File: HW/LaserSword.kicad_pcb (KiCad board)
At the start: 2 copper layers, 25 x 23 mm, 29 parts, among them J1 SWD, J2 INPUTS, J3 OUTPUTS, J4 DEBUG, Q1 Q_PNP_BEC, Q2 Q_PNP_BEC, U1 MMA7660FC, U2 DAC101S101, U3 MKE04Z8VWJ4

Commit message: Refactor to use NPN
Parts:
- Q1, Q2: value Q_PNP_BEC -> Q_NPN_BEC; moved to F.Cu
- R1, R2, R5, R7: moved to B.Cu
- moved R4 7.21 mm to (116.8, 72.3), turned to 270 degrees
- moved R3 6.89 mm to (116.8, 67.6), turned to 270 degrees
- moved R5 1.06 mm to (118.7, 72.3), turned to 90 degrees
- moved R7 1.06 mm to (120.2, 72.3), turned to 90 degrees
- moved Q2 0.91 mm to (118.7, 72.4)
- moved R2 0.82 mm to (120.2, 67.6), turned to 90 degrees
- moved R1 0.78 mm to (118.6, 67.6), turned to 90 degrees
- moved Q1 0.41 mm to (118.7, 67.7)
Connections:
- Q1 pad 2: VCC -> GND
- Q2 pad 2: VCC -> GND
- R3 pad 1: VCC -> GND
- R4 pad 1: VCC -> GND
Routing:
- net GND: track 85.9 -> 105.6 mm, vias 3 -> 5
- net VCC: track 98.7 -> 85.4 mm, vias 7 -> 6
- net /L1_OUT: track 8.88 -> 5.85 mm
- net /L2_OUT: track 13.3 -> 11.0 mm
- net /L2_uP: track 8.35 -> 10.6 mm
- net /SWCLK: track 19.9 -> 21.7 mm
- net /L1_uP: track 8.22 -> 9.94 mm
- net /SWDIO: track 9.56 -> 8.02 mm
- net /RESETn: track 14.9 -> 13.5 mm, vias 1 -> 2
- net /UART_TX: track 16.6 -> 15.6 mm
- net Net-(Q1-Pad1): track 2.17 -> 3.03 mm
- net Net-(Q2-Pad1): track 2.27 -> 2.79 mm

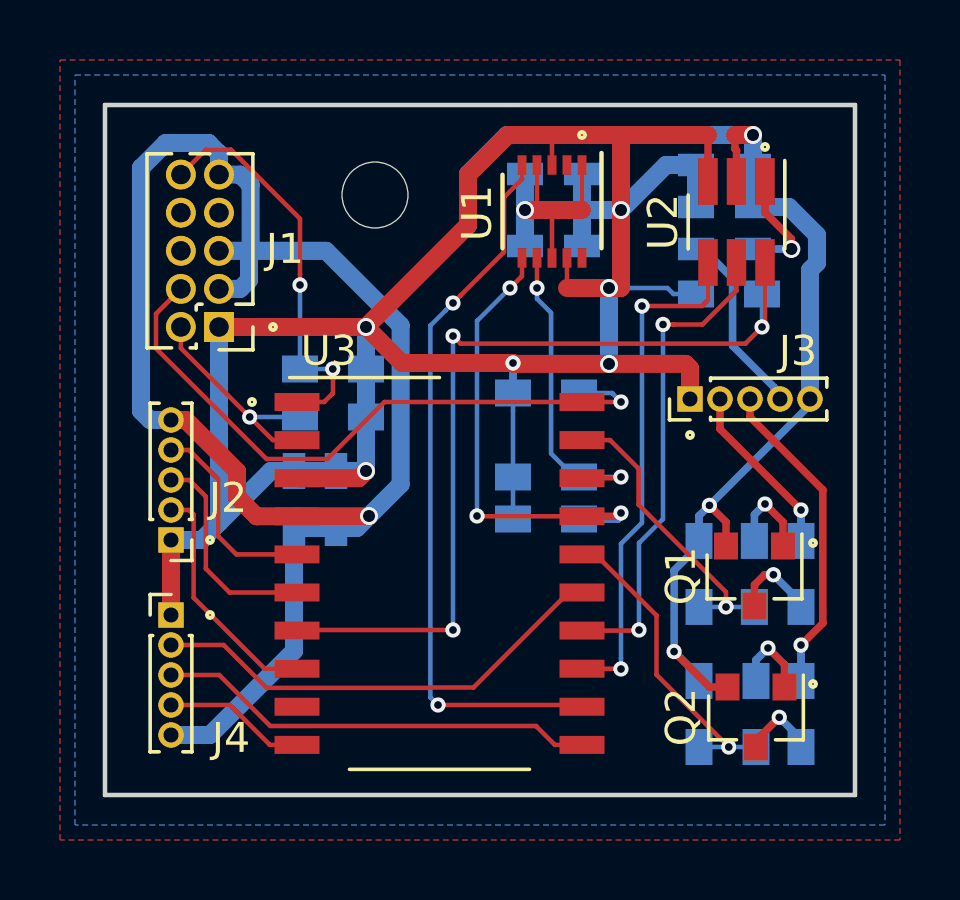
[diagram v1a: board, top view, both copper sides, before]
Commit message: Rebuilt with dual opamp, diff. speaker drive
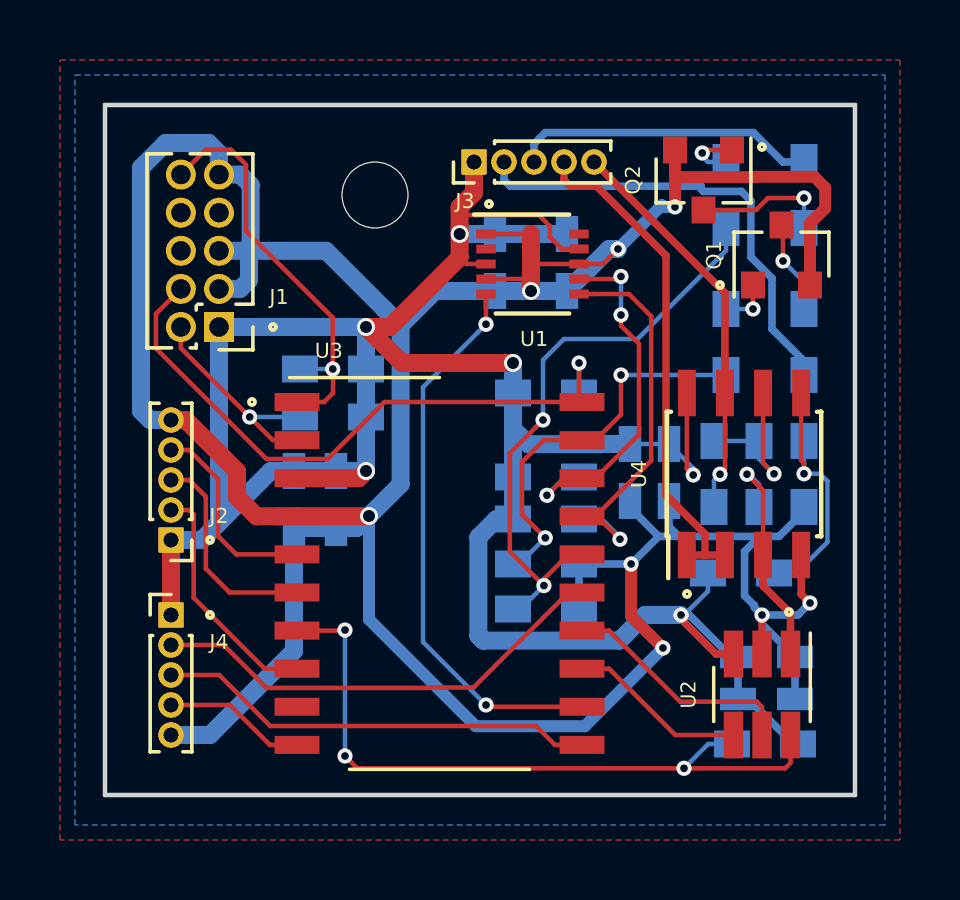
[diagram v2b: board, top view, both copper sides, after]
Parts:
- added C8: 10uF, Capacitors_SMD:C_0603_HandSoldering, B.Cu at (114.5, 64.2)
- added R13: 4.7k, Resistors_SMD:R_0603_HandSoldering, B.Cu at (118.8, 64.3)
- added R14: 4.7k, Resistors_SMD:R_0603_HandSoldering, B.Cu at (118.2, 67.6)
- added R15: 4.7k, Resistors_SMD:R_0603_HandSoldering, B.Cu at (120.3, 64.3)
- added R16: 4.7k, Resistors_SMD:R_0603_HandSoldering, B.Cu at (117.3, 64.3)
- added U4: LM358, Housings_SOIC:SOIC-8_3.9x4.9mm_Pitch1.27mm, F.Cu at (118.3, 64.3)
- C5: value 10uF -> 0.1uF
- MH1: value MountingHole_2.2mm_M2 -> MH1
- moved Q2 18.0 mm to (117.0, 54.5)
- moved R5 17.3 mm to (117.7, 55.0)
- moved R7 17.3 mm to (120.3, 55.0)
- moved C4 16.5 mm to (119.0, 70.4)
- moved C3 16.5 mm to (119.0, 71.8)
- moved U2 15.8 mm to (118.9, 71.7)
- moved R12 15.0 mm to (119.0, 73.3), turned to 180 degrees
- moved Q1 10.7 mm to (119.5, 57.0), turned to 90 degrees
- moved J3 10.7 mm to (109.3, 53.9)
- moved R1 7.79 mm to (117.7, 59.9)
- moved R2 7.73 mm to (120.3, 59.9), turned to 270 degrees
- moved C5 7.68 mm to (115.8, 64.2), turned to 270 degrees
- moved R4 6.19 mm to (111.7, 68.8), turned to 180 degrees
- moved R3 5.11 mm to (111.7, 67.3), turned to 180 degrees
- moved C2 3.54 mm to (110.0, 57.2), turned to 270 degrees
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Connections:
- C5 pad 1: /SPKR -> VCC
- C5 pad 2: Net-(C5-Pad2) -> GND
- J1 pad 6: Net-(J1-Pad6) -> (no net)
- J1 pad 7: Net-(J1-Pad7) -> (no net)
- J1 pad 8: Net-(J1-Pad8) -> (no net)
- J3 pad 4: /SPKR -> /SPKR_P
- J3 pad 5: GND -> /SPKR_N
- U1 pad 10: Net-(U1-Pad10) -> (no net)
- U1 pad 2: Net-(U1-Pad2) -> (no net)
- U2 pad 1: Net-(C5-Pad2) -> /DAC_OUT
- U3 pad 9: Net-(U3-Pad9) -> (no net)
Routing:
- net GND: track 105.6 -> 125.4 mm, vias 5 -> 8
- net /SPKR_P: track 0.00 -> 16.8 mm
- net /SPKR_N: track 0.00 -> 13.5 mm, vias 0 -> 1
- net /SPI_MOSI: track 17.2 -> 5.97 mm, vias 2 -> 0
- net /L1_OUT: track 5.85 -> 15.7 mm, vias 1 -> 0
- net /L2_uP: track 10.6 -> 20.4 mm, vias 1 -> 2
- net Net-(R14-Pad1): track 0.00 -> 8.95 mm, vias 0 -> 1
- net /SPI_CLK: track 16.3 -> 7.99 mm, vias 2 -> 0
- net /DAC_OUT: track 0.00 -> 7.89 mm, vias 0 -> 1
- net /SPKR: track 6.30 -> 0.00 mm
- net Net-(R13-Pad1): track 0.00 -> 5.65 mm, vias 0 -> 1
- net /ACCEL_INTn: track 24.2 -> 18.7 mm
- net /SPI_CSn: track 28.9 -> 23.8 mm
- net Net-(C5-Pad2): track 3.89 -> 0.00 mm, vias 1 -> 0
- net VCC: track 85.4 -> 88.8 mm
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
